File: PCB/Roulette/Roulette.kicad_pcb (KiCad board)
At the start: 2 copper layers, 130 x 130 mm, 266 parts, among them J1 USB-PROG, J2 Shelly, J3 Conn_01x03, J4 Conn_01x02, Q1 PMF170XP,115, SW1 SW_Push, SW2 SW_Push, U1 ESP32-S3-MINI-1

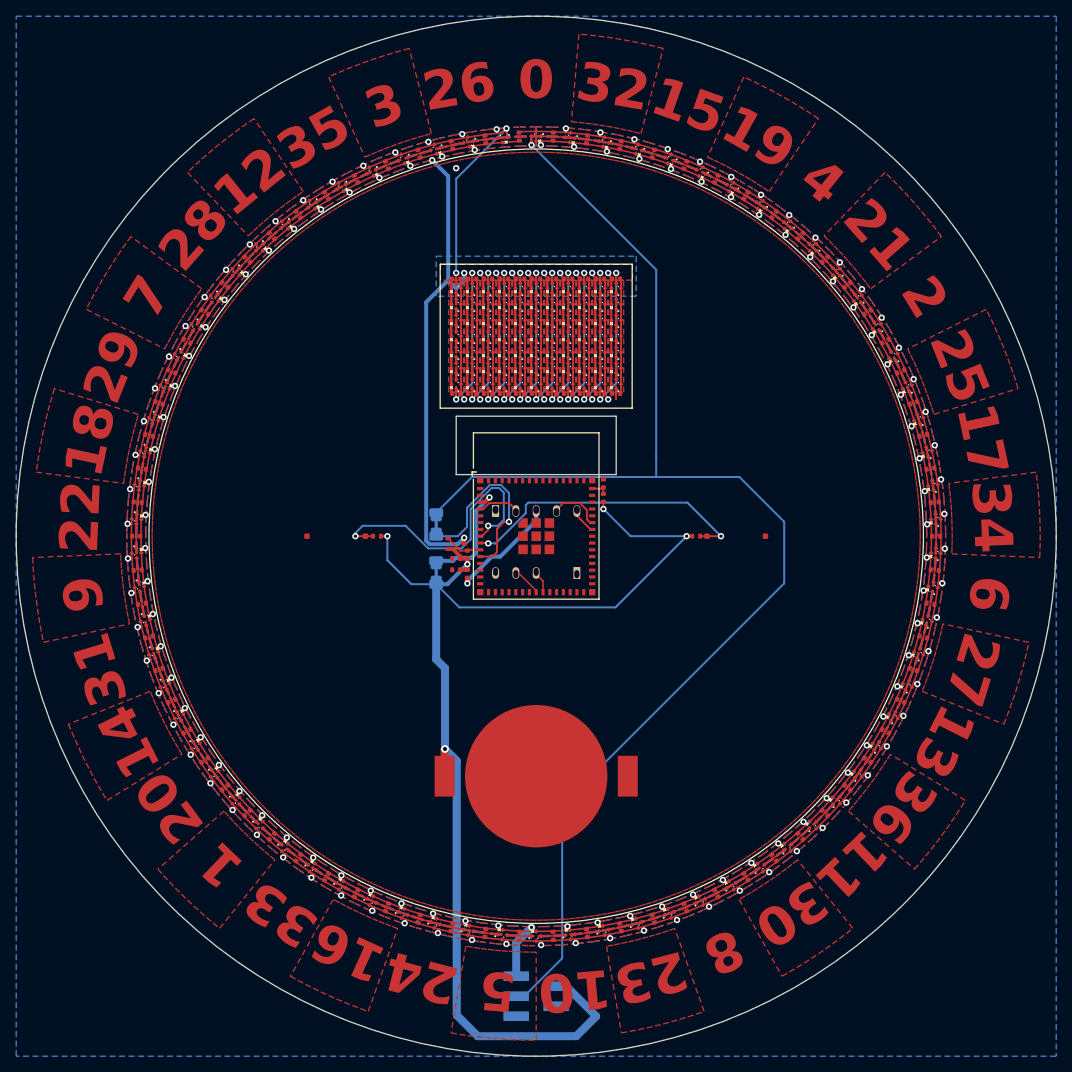
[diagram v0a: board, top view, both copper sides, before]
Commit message: Started new h/w - needs parts and tracking
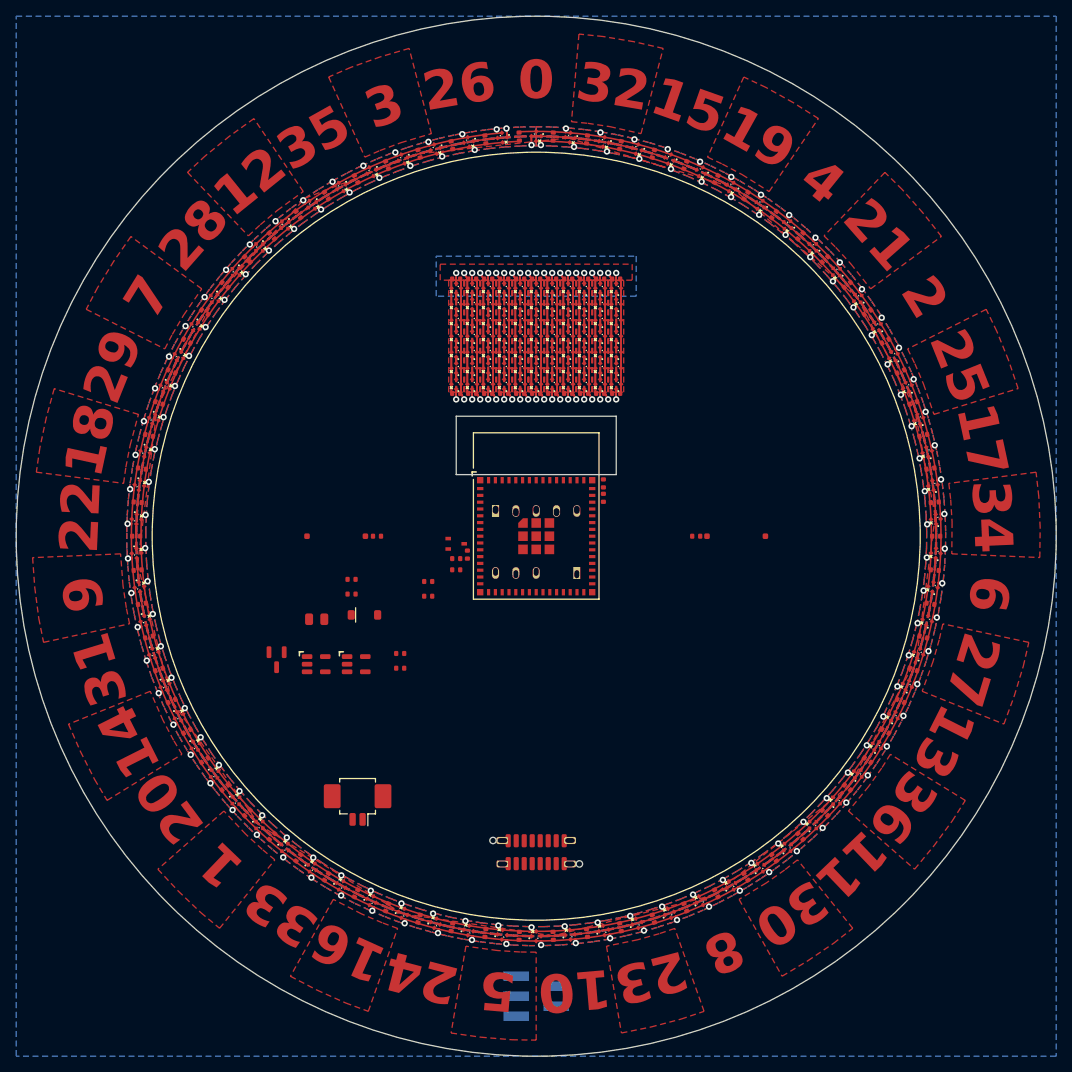
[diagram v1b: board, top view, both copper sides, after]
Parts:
- removed BT1: Battery_Cell, RevK:Battery-Holder-2032
- removed JP1, JP2: Jumper_2_Bridged, RevK:Pad_1206_0805_Bridged
- added C100: 4.7uF/50V, RevK:C_0805, F.Cu at (72.7, 110.4)
- added D152: MBR0530, RevK:D_SOD-123, F.Cu at (78.5, 109.8)
- added J5: Battery, Connector_Molex:Molex_PicoBlade_53261-0271_1x02-1MP_P1.25mm_Horizontal, F.Cu at (77.7, 133.0)
- added J6: USB_C_Receptacle_USB2.0, RevK:USB_C_G_Switch-7082C, F.Cu at (100.0, 139.5)
- added Q2: CJ2301, RevK:SOT-23, F.Cu at (67.5, 115.4)
- added R10: 100K, RevK:R_0402, F.Cu at (76.9, 107.2)
- added R6: 10K, RevK:R_0402, F.Cu at (83.0, 114.7)
- added R7: 10K, RevK:R_0402, F.Cu at (83.0, 116.5)
- added R8: 5K1, RevK:R_0402, F.Cu at (86.5, 107.5)
- added R9: 100K, RevK:R_0402, F.Cu at (76.9, 105.4)
- added U2: TP4054, RevK:SOT-23-5, F.Cu at (72.5, 116.0)
- added U3: ME6211C33M5G-N, RevK:SOT-23-5, F.Cu at (77.5, 116.0)
- R3: value 100R -> 5K1
- moved R3 4.99 mm to (86.5, 105.7), turned to 0 degrees
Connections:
- C97 pad 1: VBAT -> +3V3
- C98 pad 1: VBAT -> +3V3
- Q1 pad 2: VBAT -> +3V3
- R1 pad 1: VBAT -> +3V3
- R2 pad 1: VBAT -> +3V3
- R3 pad 1: VBAT -> GND
- R3 pad 2: +3V3 -> Net-(J6-CC1)
- R4 pad 1: VBAT -> +3V3
- R5 pad 1: VBAT -> +3V3
- U1 pad 11: Net-(JP1-A) -> LED
- U1 pad 12: unconnected-(U1-GPIO8-Pad12) -> ADC
- U1 pad 13: unconnected-(U1-GPIO9-Pad13) -> STAT
- U1 pad 3: Net-(JP2-B) -> +3V3
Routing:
- net GND: track 907.3 -> 720.2 mm, vias 84 -> 83
- net VLED: track 893.2 -> 712.7 mm, vias 85 -> 83
- net LED: track 172.7 -> 2.20 mm
- net VBAT: track 155.5 -> 0.00 mm, vias 5 -> 0
- net BUTTON2: track 37.2 -> 0.00 mm, vias 2 -> 0
- net BUTTON1: track 35.8 -> 0.00 mm, vias 2 -> 0
- net Net-(JP1-A): track 24.3 -> 0.00 mm, vias 1 -> 0
- net Net-(D74-O): track 27.9 -> 4.80 mm
- net Net-(D95-O): track 24.4 -> 5.20 mm
- net Net-(D88-O): track 24.4 -> 5.20 mm
- net Net-(D81-O): track 24.4 -> 5.20 mm
- net Net-(D137-O): track 24.4 -> 5.20 mm
- net Net-(D130-O): track 24.4 -> 5.20 mm
- net Net-(D123-O): track 24.4 -> 5.20 mm
- net Net-(D116-O): track 24.4 -> 5.20 mm
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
